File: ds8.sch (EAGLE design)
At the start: 85 parts, among them IC1 TM4C1230C3PM, IC2 TPS77333, Q1 BC850, Q2 BC850, Q3 BC850, U1 LM13700M, U2 LM324, U3 LM324, U4 LM741D

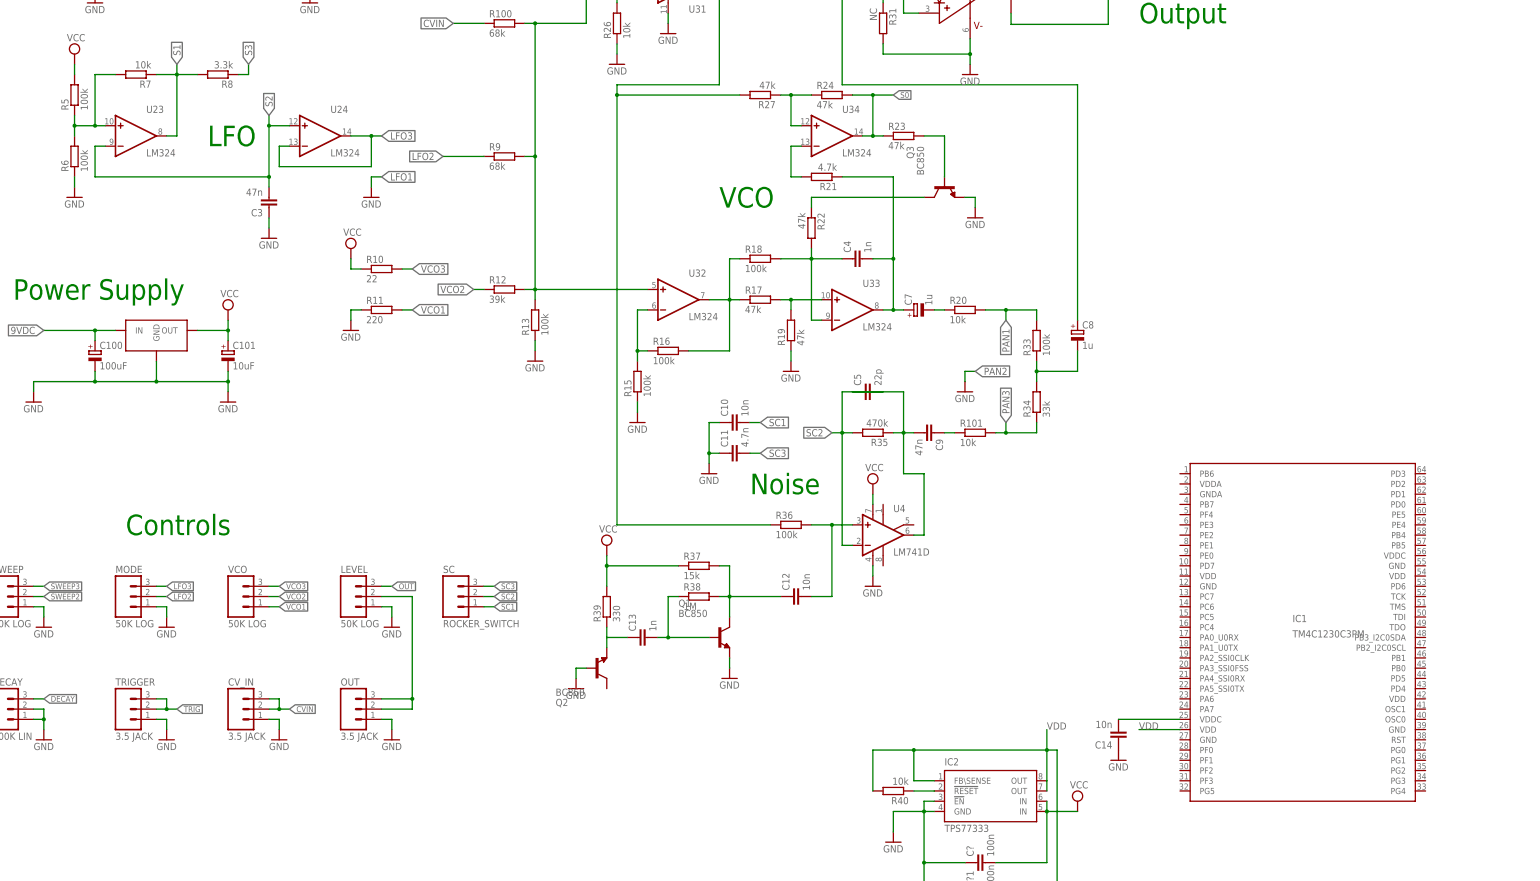
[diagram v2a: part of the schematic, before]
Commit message: added dac
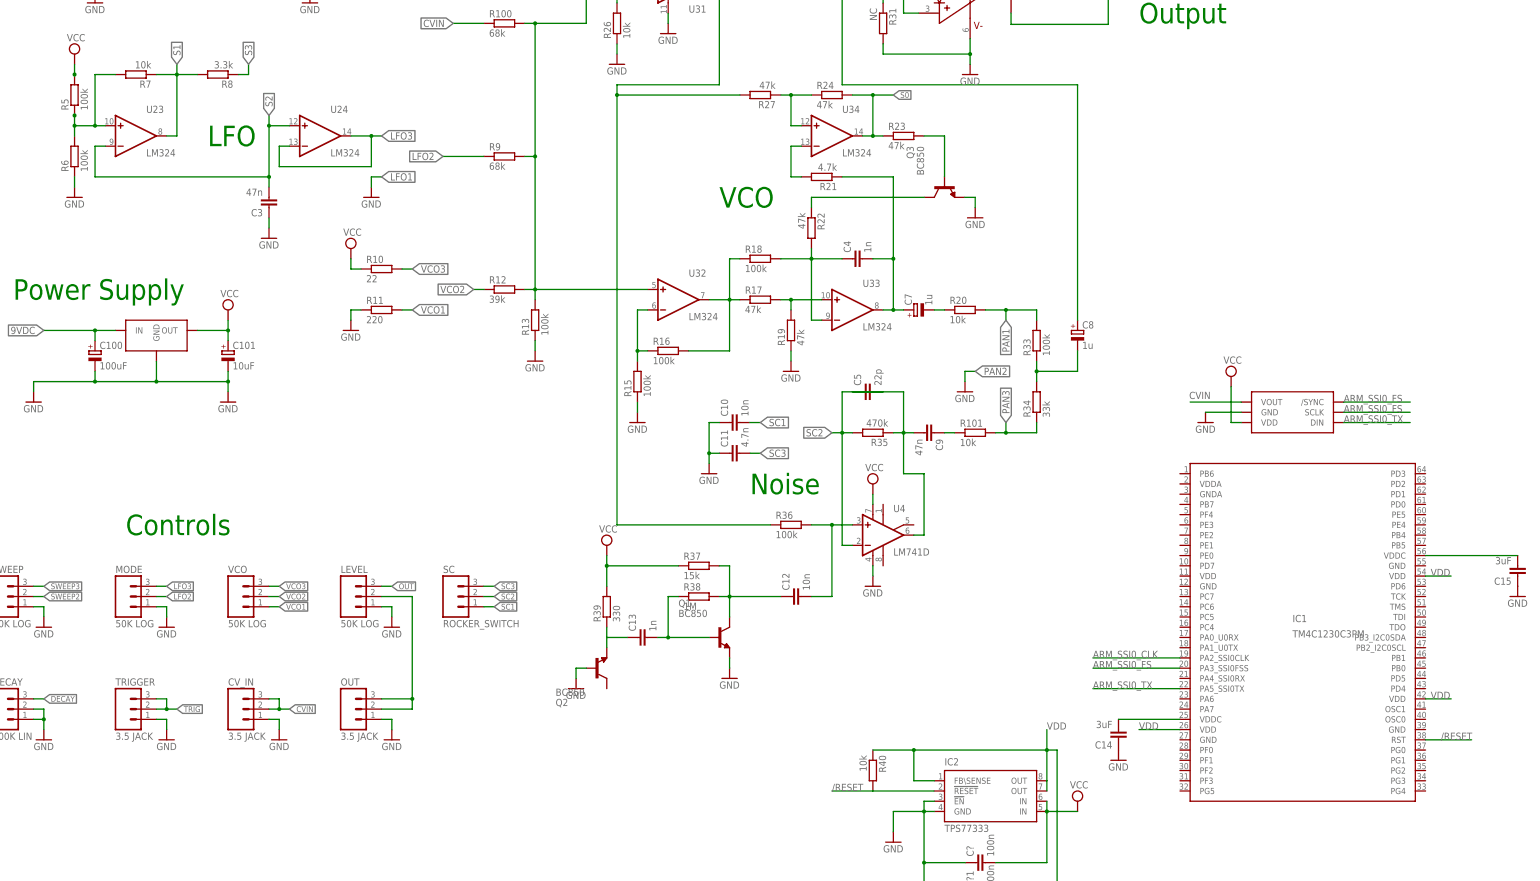
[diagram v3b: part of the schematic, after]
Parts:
- added C15: 3uF, rcl:C-EUC1206
- added U$1: DAC7512, ds8:DAC7512
- C14: value 10n -> 3uF
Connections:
- new net /RESET: IC1.RST, IC2.!RESET, R40.2
- new net ARM_SSI0_CLK: IC1.PA2_SSI0CLK
- new net ARM_SSI0_FS: IC1.PA3_SSI0FSS, U$1./SYNC, U$1.SCLK
- new net ARM_SSI0_TX: IC1.PA5_SSI0TX, U$1.DIN
- new net N$26: C15.2
- new net N$35: IC1.VDD@3
- net CVIN: now also U$1.VOUT
- net GND: now also C15.1, U$1.GND
- net N$18: now also IC1.VDD@2; no longer IC2.!RESET, R40.1
- net VCC: now also U$1.VDD
- net VDD: now also R40.1; no longer R40.2
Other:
- moved on the sheet: R40
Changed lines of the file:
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@@
 <setting verticaltext="up"/>
 </settings>
-<grid distance="0.1" unitdist="inch" unit="inch" style="lines" multiple="1" display="no" altdistance="0.01" altunitdist="inch" altunit="inch"/>
+<grid distance="0.05" unitdist="inch" unit="inch" style="lines" multiple="1" display="no" altdistance="0.01" altunitdist="inch" altunit="inch"/>
 <layers>
 <layer number="1" name="Top" color="4" fill="1" visible="no" active="no"/>
@@
 <part name="C?1" library="rcl" deviceset="C-EU" device="C1206" value="100n"/>
 <part name="R40" library="rcl" deviceset="R-EU_" device="M0805" value="10k"/>
-<part name="C14" library="rcl" deviceset="C-EU" device="C1206" value="10n"/>
+<part name="C14" library="rcl" deviceset="C-EU" device="C1206" value="3uF"/>
 <part name="GND33" library="supply1" deviceset="GND" device=""/>
+<part name="GND34" library="supply1" deviceset="GND" device=""/>
+<part name="U$1" library="ds8" deviceset="DAC7512" device=""/>
+<part name="SUPPLY11" library="supply2" deviceset="VCC" device=""/>
+<part name="C15" library="rcl" deviceset="C-EU" device="C1206" value="3uF"/>
+<part name="GND35" library="supply1" deviceset="GND" device=""/>
 </parts>
 <sheets>
@@
 <instance part="C?" gate="G$1" x="213.36" y="-203.2" rot="R90"/>
 <instance part="C?1" gate="G$1" x="213.36" y="-210.82" rot="R90"/>
-<instance part="R40" gate="G$1" x="193.04" y="-185.42" rot="R180"/>
+<instance part="R40" gate="G$1" x="187.96" y="-180.34" rot="R270"/>
 <instance part="C14" gate="G$1" x="248.92" y="-172.72" rot="R180"/>
 <instance part="GND33" gate="1" x="248.92" y="-177.8"/>
+<instance part="GND34" gate="1" x="270.51" y="-93.98"/>
+<instance part="U$1" gate="G$1" x="292.1" y="-91.44"/>
+<instance part="SUPPLY11" gate="G$1" x="276.86" y="-82.55"/>
+<instance part="C15" gate="G$1" x="347.98" y="-132.08" rot="R180"/>
+<instance part="GND35" gate="1" x="347.98" y="-137.16"/>
 </instances>
 <busses>
@@
 <pinref part="GND33" gate="1" pin="GND"/>
 </segment>
+<segment>
+<pinref part="GND34" gate="1" pin="GND"/>
+<wire x1="270.51" y1="-91.44" x2="279.4" y2="-91.44" width="0.1524" layer="91"/>
+<pinref part="U$1" gate="G$1" pin="GND"/>
+</segment>
+<segment>
+<pinref part="C15" gate="G$1" pin="1"/>
+<pinref part="GND35" gate="1" pin="GND"/>
+</segment>
 </net>
 <net name="VCC" class="0">
@@
 <pinref part="R5" gate="G$1" pin="1"/>
 <wire x1="-10.16" y1="-5.08" x2="-10.16" y2="-7.62" width="0.1524" layer="91"/>
+<junction x="-10.16" y="-17.78"/>
 </segment>
 <segment>
@@
 <wire x1="231.14" y1="-203.2" x2="218.44" y2="-203.2" width="0.1524" layer="91"/>
 <junction x="231.14" y="-190.5"/>
+</segment>
+<segment>
+<pinref part="SUPPLY11" gate="G$1" pin="VCC"/>
+<wire x1="276.86" y1="-85.09" x2="276.86" y2="-93.98" width="0.1524" layer="91"/>
+<pinref part="U$1" gate="G$1" pin="VDD"/>
+<wire x1="276.86" y1="-93.98" x2="279.4" y2="-93.98" width="0.1524" layer="91"/>
 </segment>
 </net>
@@
 <junction x="-5.08" y="-20.32"/>
 <junction x="-10.16" y="-20.32"/>
+<junction x="-10.16" y="-7.62"/>
 </segment>
 </net>
@@
 <label x="43.18" y="-165.1" size="1.4224" layer="95" xref="yes"/>
 </segment>
+<segment>
+<wire x1="279.4" y1="-88.9" x2="266.7" y2="-88.9" width="0.1524" layer="91"/>
+<label x="271.78" y="-86.36" size="1.778" layer="95" rot="R180"/>
+<pinref part="U$1" gate="G$1" pin="VOUT"/>
+</segment>
 </net>
 <net name="LFO2" class="0">
@@
 <wire x1="233.68" y1="-210.82" x2="233.68" y2="-175.26" width="0.1524" layer="91"/>
 <wire x1="233.68" y1="-175.26" x2="231.14" y2="-175.26" width="0.1524" layer="91"/>
-<pinref part="R40" gate="G$1" pin="2"/>
-<wire x1="187.96" y1="-185.42" x2="187.96" y2="-175.26" width="0.1524" layer="91"/>
 <wire x1="187.96" y1="-175.26" x2="198.12" y2="-175.26" width="0.1524" layer="91"/>
 <junction x="198.12" y="-175.26"/>
+<pinref part="R40" gate="G$1" pin="1"/>
 </segment>
 <segment>
@@
 <label x="254" y="-170.18" size="1.778" layer="95"/>
 <wire x1="254" y1="-170.18" x2="264.16" y2="-170.18" width="0.1524" layer="91"/>
-</segment>
-</net>
-<net name="N$18" class="0">
-<segment>
-<pinref part="IC2" gate="G$1" pin="!RESET"/>
-<pinref part="R40" gate="G$1" pin="1"/>
-<wire x1="203.2" y1="-185.42" x2="198.12" y2="-185.42" width="0.1524" layer="91"/>
+<label x="326.39" y="-132.08" size="1.778" layer="95"/>
+<label x="326.39" y="-162.56" size="1.778" layer="95"/>
 </segment>
 </net>
@@
 </segment>
 </net>
+<net name="ARM_SSI0_FS" class="0">
+<segment>
+<pinref part="IC1" gate="G$1" pin="PA3_SSI0FSS"/>
+<wire x1="264.16" y1="-154.94" x2="242.57" y2="-154.94" width="0.1524" layer="91"/>
+<label x="242.57" y="-154.94" size="1.778" layer="95"/>
+</segment>
+<segment>
+<pinref part="U$1" gate="G$1" pin="/SYNC"/>
+<wire x1="304.8" y1="-88.9" x2="321.31" y2="-88.9" width="0.1524" layer="91"/>
+<label x="304.8" y="-88.9" size="1.778" layer="95"/>
+</segment>
+<segment>
+<pinref part="U$1" gate="G$1" pin="SCLK"/>
+<wire x1="304.8" y1="-91.44" x2="321.31" y2="-91.44" width="0.1524" layer="91"/>
+<label x="304.8" y="-91.44" size="1.778" layer="95"/>
+</segment>
+</net>
+<net name="ARM_SSI0_CLK" class="0">
+<segment>
+<pinref part="IC1" gate="G$1" pin="PA2_SSI0CLK"/>
+<wire x1="264.16" y1="-152.4" x2="242.57" y2="-152.4" width="0.1524" layer="91"/>
+<label x="242.57" y="-152.4" size="1.778" layer="95"/>
+</segment>
+</net>
+<net name="ARM_SSI0_TX" class="0">
+<segment>
+<pinref part="IC1" gate="G$1" pin="PA5_SSI0TX"/>
+<wire x1="264.16" y1="-160.02" x2="242.57" y2="-160.02" width="0.1524" layer="91"/>
+<label x="242.57" y="-160.02" size="1.778" layer="95"/>
+</segment>
+<segment>
+<pinref part="U$1" gate="G$1" pin="DIN"/>
+<wire x1="304.8" y1="-93.98" x2="321.31" y2="-93.98" width="0.1524" layer="91"/>
+<label x="304.8" y="-93.98" size="1.778" layer="95"/>
+</segment>
+</net>
+<net name="/RESET" class="0">
+<segment>
+<pinref part="IC2" gate="G$1" pin="!RESET"/>
+<pinref part="R40" gate="G$1" pin="2"/>
+<wire x1="203.2" y1="-185.42" x2="187.96" y2="-185.42" width="0.1524" layer="91"/>
+<wire x1="187.96" y1="-185.42" x2="177.8" y2="-185.42" width="0.1524" layer="91"/>
+<label x="177.8" y="-185.42" size="1.778" layer="95"/>
+</segment>
+<segment>
+<pinref part="IC1" gate="G$1" pin="RST"/>
+<wire x1="325.12" y1="-172.72" x2="336.55" y2="-172.72" width="0.1524" layer="91"/>
+<label x="328.93" y="-172.72" size="1.778" layer="95"/>
+</segment>
+</net>
+<net name="N$18" class="0">
+<segment>
+<pinref part="IC1" gate="G$1" pin="VDD@2"/>
+<wire x1="325.12" y1="-162.56" x2="331.47" y2="-162.56" width="0.1524" layer="91"/>
+</segment>
+</net>
+<net name="N$26" class="0">
+<segment>
+<pinref part="C15" gate="G$1" pin="2"/>
+<wire x1="325.12" y1="-127" x2="347.98" y2="-127" width="0.1524" layer="91"/>
+</segment>
+</net>
+<net name="N$35" class="0">
+<segment>
+<pinref part="IC1" gate="G$1" pin="VDD@3"/>
+<wire x1="325.12" y1="-132.08" x2="331.47" y2="-132.08" width="0.1524" layer="91"/>
+</segment>
+</net>

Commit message: clean up
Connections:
- removed net N$18: IC1.VDD@2
- removed net N$35: IC1.VDD@3
- net GND: now also IC1.GND@0, IC1.GND@2, IC1.GND@3, IC1.GNDA
- net N$5: no longer R5.2
- net VCC: now also R5.2; no longer R5.1
- net VDD: now also IC1.VDD@0, IC1.VDD@2, IC1.VDD@3, IC1.VDDA
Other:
- moved on the sheet: C5, R5

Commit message: wire conflicts
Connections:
- net GND: now also IC1.GND@1
- net N$36: now also IC1.VDDC@1
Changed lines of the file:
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@@
 <instance part="VDD6" gate="G$1" x="259.08" y="-129.54"/>
 <instance part="GND38" gate="1" x="254" y="-138.43"/>
-<instance part="GND39" gate="1" x="335.28" y="-132.08"/>
+<instance part="GND39" gate="1" x="336.55" y="-132.08"/>
 <instance part="GND40" gate="1" x="342.9" y="-172.72"/>
 </instances>
@@
 <pinref part="GND36" gate="1" pin="GND"/>
 <wire x1="256.54" y1="-172.72" x2="256.54" y2="-175.26" width="0.1524" layer="91"/>
+<pinref part="IC1" gate="G$1" pin="GND@1"/>
 </segment>
 <segment>
@@
 <pinref part="IC1" gate="G$1" pin="GND@3"/>
 <pinref part="GND39" gate="1" pin="GND"/>
-<wire x1="325.12" y1="-129.54" x2="335.28" y2="-129.54" width="0.1524" layer="91"/>
+<wire x1="325.12" y1="-129.54" x2="336.55" y2="-129.54" width="0.1524" layer="91"/>
 </segment>
 <segment>
@@
 <net name="PAN2" class="0">
 <segment>
-<wire x1="213.36" y1="-81.28" x2="210.82" y2="-81.28" width="0.1524" layer="91"/>
+<wire x1="214.63" y1="-81.28" x2="210.82" y2="-81.28" width="0.1524" layer="91"/>
 <wire x1="210.82" y1="-81.28" x2="210.82" y2="-83.82" width="0.1524" layer="91"/>
-<label x="213.36" y="-81.28" size="1.778" layer="95" xref="yes"/>
+<label x="214.63" y="-81.28" size="1.778" layer="95" xref="yes"/>
 <pinref part="GND11" gate="1" pin="GND"/>
 </segment>
@@
 <pinref part="C15" gate="G$1" pin="2"/>
 <wire x1="325.12" y1="-127" x2="347.98" y2="-127" width="0.1524" layer="91"/>
+<pinref part="IC1" gate="G$1" pin="VDDC@1"/>
 </segment>
 </net>
@@
 </sheet>
 </sheets>
+<errors>
+</errors>
 </schematic>
 </drawing>

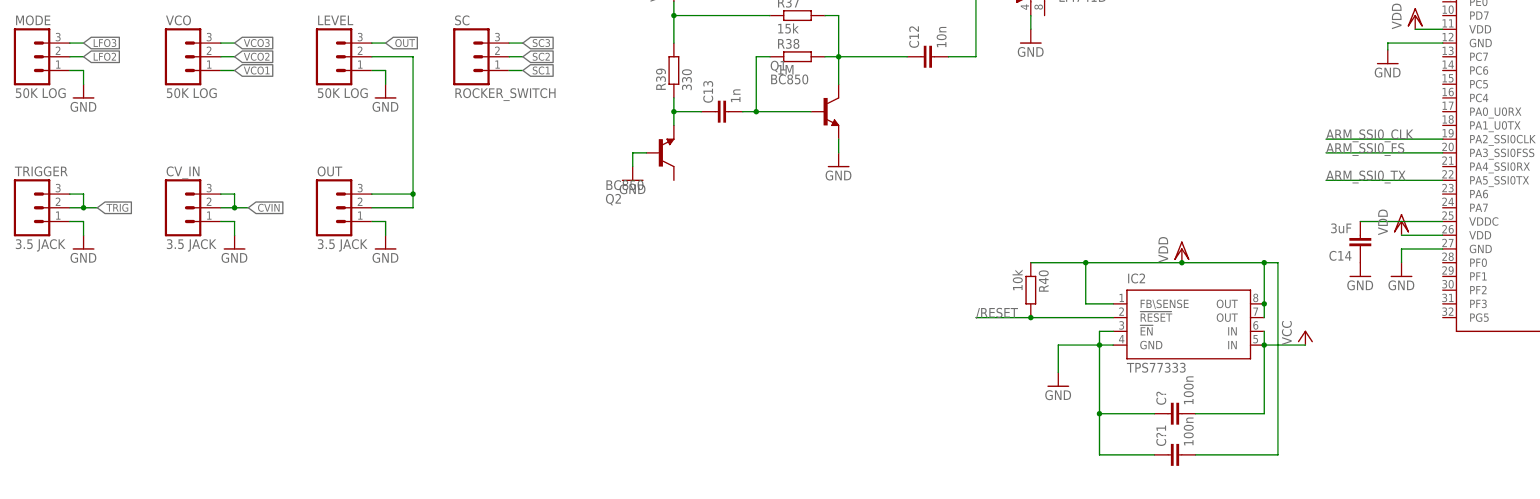
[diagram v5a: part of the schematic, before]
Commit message: added optocoupler
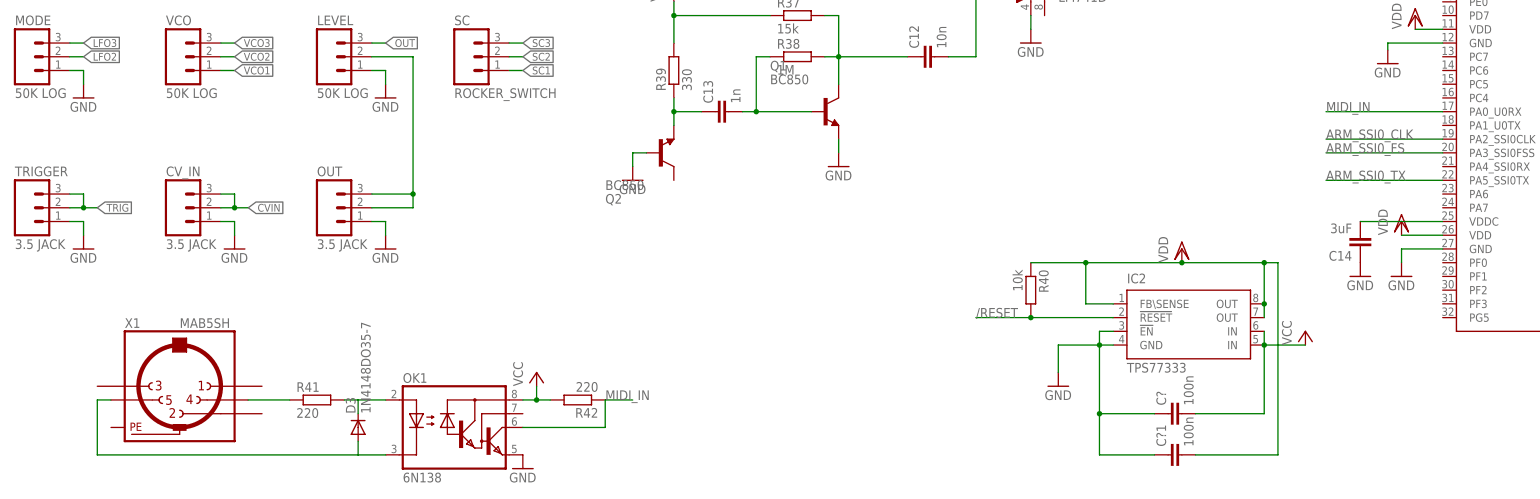
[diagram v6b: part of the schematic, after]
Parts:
- added D3: 1N4148DO35-7, diode:1N4148DO35-7
- added OK1: 6N138, optocoupler:6N138
- added R41, R42: 220, rcl:R-EU_R0805
- added X1: MAB5SH, con-hirschmann:MAB5SH
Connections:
- new net MIDI_IN: IC1.PA0_U0RX, OK1.VO, R42.1
- new net N$18: R41.1, X1.4
- new net N$26: D3.C, OK1.A, R41.2
- new net N$35: D3.A, OK1.C, X1.5
- net GND: now also OK1.GND
- net VCC: now also OK1.VCC, R42.2
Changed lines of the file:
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@@
 <part name="GND39" library="supply1" deviceset="GND" device=""/>
 <part name="GND40" library="supply1" deviceset="GND" device=""/>
+<part name="X1" library="con-hirschmann" deviceset="MAB5SH" device=""/>
+<part name="OK1" library="optocoupler" deviceset="6N138" device=""/>
+<part name="P+12" library="supply1" deviceset="VCC" device=""/>
+<part name="R41" library="rcl" deviceset="R-EU_" device="R0805" value="220"/>
+<part name="D3" library="diode" deviceset="1N4148" device="DO35-7"/>
+<part name="R42" library="rcl" deviceset="R-EU_" device="R0805" value="220"/>
+<part name="GND41" library="supply1" deviceset="GND" device=""/>
 </parts>
 <sheets>
@@
 <instance part="GND39" gate="1" x="336.55" y="-132.08"/>
 <instance part="GND40" gate="1" x="342.9" y="-172.72"/>
+<instance part="X1" gate="G$1" x="30.48" y="-198.12"/>
+<instance part="OK1" gate="G$1" x="81.28" y="-205.74"/>
+<instance part="P+12" gate="VCC" x="96.52" y="-195.58"/>
+<instance part="R41" gate="G$1" x="55.88" y="-200.66"/>
+<instance part="D3" gate="G$1" x="63.5" y="-205.74" rot="R90"/>
+<instance part="R42" gate="G$1" x="104.14" y="-200.66" rot="R180"/>
+<instance part="GND41" gate="1" x="93.98" y="-213.36"/>
 </instances>
 <busses>
@@
 <wire x1="325.12" y1="-170.18" x2="342.9" y2="-170.18" width="0.1524" layer="91"/>
 </segment>
+<segment>
+<pinref part="OK1" gate="G$1" pin="GND"/>
+<pinref part="GND41" gate="1" pin="GND"/>
+</segment>
 </net>
 <net name="VCC" class="0">
@@
 <wire x1="276.86" y1="-93.98" x2="279.4" y2="-93.98" width="0.1524" layer="91"/>
 <pinref part="P+9" gate="VCC" pin="VCC"/>
+</segment>
+<segment>
+<pinref part="R42" gate="G$1" pin="2"/>
+<pinref part="OK1" gate="G$1" pin="VCC"/>
+<wire x1="99.06" y1="-200.66" x2="96.52" y2="-200.66" width="0.1524" layer="91"/>
+<pinref part="P+12" gate="VCC" pin="VCC"/>
+<wire x1="96.52" y1="-200.66" x2="93.98" y2="-200.66" width="0.1524" layer="91"/>
+<wire x1="96.52" y1="-198.12" x2="96.52" y2="-200.66" width="0.1524" layer="91"/>
+<junction x="96.52" y="-200.66"/>
 </segment>
 </net>
@@
 </segment>
 </net>
+<net name="N$18" class="0">
+<segment>
+<pinref part="X1" gate="G$1" pin="4"/>
+<pinref part="R41" gate="G$1" pin="1"/>
+<wire x1="43.18" y1="-200.66" x2="50.8" y2="-200.66" width="0.1524" layer="91"/>
+</segment>
+</net>
+<net name="N$26" class="0">
+<segment>
+<pinref part="R41" gate="G$1" pin="2"/>
+<pinref part="OK1" gate="G$1" pin="A"/>
+<wire x1="60.96" y1="-200.66" x2="63.5" y2="-200.66" width="0.1524" layer="91"/>
+<pinref part="D3" gate="G$1" pin="C"/>
+<wire x1="63.5" y1="-200.66" x2="68.58" y2="-200.66" width="0.1524" layer="91"/>
+<wire x1="63.5" y1="-203.2" x2="63.5" y2="-200.66" width="0.1524" layer="91"/>
+</segment>
+</net>
+<net name="N$35" class="0">
+<segment>
+<pinref part="OK1" gate="G$1" pin="C"/>
+<wire x1="68.58" y1="-210.82" x2="63.5" y2="-210.82" width="0.1524" layer="91"/>
+<wire x1="63.5" y1="-210.82" x2="15.24" y2="-210.82" width="0.1524" layer="91"/>
+<wire x1="15.24" y1="-210.82" x2="15.24" y2="-200.66" width="0.1524" layer="91"/>
+<pinref part="X1" gate="G$1" pin="5"/>
+<wire x1="15.24" y1="-200.66" x2="17.78" y2="-200.66" width="0.1524" layer="91"/>
+<pinref part="D3" gate="G$1" pin="A"/>
+<wire x1="63.5" y1="-208.28" x2="63.5" y2="-210.82" width="0.1524" layer="91"/>
+</segment>
+</net>
+<net name="MIDI_IN" class="0">
+<segment>
+<pinref part="OK1" gate="G$1" pin="VO"/>
+<wire x1="93.98" y1="-205.74" x2="109.22" y2="-205.74" width="0.1524" layer="91"/>
+<pinref part="R42" gate="G$1" pin="1"/>
+<wire x1="109.22" y1="-205.74" x2="109.22" y2="-200.66" width="0.1524" layer="91"/>
+<wire x1="109.22" y1="-200.66" x2="114.3" y2="-200.66" width="0.1524" layer="91"/>
+<label x="109.22" y="-200.66" size="1.778" layer="95"/>
+</segment>
+<segment>
+<pinref part="IC1" gate="G$1" pin="PA0_U0RX"/>
+<wire x1="264.16" y1="-147.32" x2="242.57" y2="-147.32" width="0.1524" layer="91"/>
+<label x="242.57" y="-147.32" size="1.778" layer="95"/>
+</segment>
+</net>
